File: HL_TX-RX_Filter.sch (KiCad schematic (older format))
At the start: 167 parts, among them J1 ICSP, Q1 2N7002, Q2 2N7002, Q3 2N7002, Q4 2N7002, Q5 2N7002, Q6 2N7002, Q7 2N7002, Q8 2N7002, U1 LD1117S33TR, U10 PE4259, U11 PE4259, U12 PE4259, U13 PE4259, U14 PE4259, U2 ATMEGA328-AU, U3 PE4259, U4 PE4259, U5 PE4259, U6 PE4259, U7 PE4259, U8 PE4259, U9 PE4259

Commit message: Changes to ISP wiring
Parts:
- removed D18: D_Schottky, symbol D_Schottky
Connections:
- net labels added: +3v3
- net labels removed: +5V
- wire segments 314 -> 315
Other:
- moved on the sheet: C37, C38, C39, C40, C41, C42, C43, C44, C45, C46, C47, C48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

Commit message: Corrections and further additions
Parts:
- removed U9: PE4259, symbol PE4259
- added J1: To Antenna, symbol CONN_01X02
- added J2: From Tx, symbol CONN_01X02
- added J4: To Rx in, symbol CONN_01X02
- C1: value C -> 30pF
- C10: value C -> 1000p
- C11: value C -> 15p
- C12: value C -> 39p
- C13: value C -> 68p
- C14: value C -> 82p
- C15, C28: value C -> 180p
- C16: value C -> 200p
- C17: value C -> 300p
- C18: value C -> 560p
- C19: value C -> 1082p
- C2: value C -> 78pF
- C20: value C -> 2100p
- C21: value C -> 43p
- C22: value C -> 130p
- C23: value C -> 220p
- C24: value C -> 270p
- C25: value C -> 552p
- C26: value C -> 74p
- C27: value C -> 120p
- C29: value C -> 390p
- C3: value C -> 56pF
- C30: value C -> 736p
- C39: renamed from C36; value C -> 0.1u
- C4: value C -> 150pF
- C40: renamed from C37; value C -> 3000p
- C41: renamed from C38; value C -> 0.012u
- C42: renamed from C39; value C -> 1600p
- C43: renamed from C40; value C -> 1500p
- C47: renamed from C44; value C -> 2400p
- C48: renamed from C45; value C -> 8200p
- C5: value C -> 10pF
- C52: renamed from C49; value C -> 1800p
- C53: renamed from C50; value C -> 680p
- C57: renamed from C54; value C -> 3000p
- C58: renamed from C55; value C -> 2700p
- C6: value C -> 100p
- C62: renamed from C59; value C -> 2400p
- C63: renamed from C60; value C -> 2000p
- C7: value C -> 150p
- C8: value C -> 280p
- C9: value C -> 540p
- L1: value L -> T37-10 10t
- L10: value L -> Choke
- L15: value L -> 11t
- L16, L4: value L -> 12t
- L17, L5: value L -> 15t
- L19, L26: value L -> 34t
- L2: value L -> T37-10 11t
- L25: value L -> 28t
- L27: value L -> 20t
- L31: value L -> 35t
- L32: value L -> 23t
- L6: value L -> 18t
- L8: value L -> 39t
- renumbered C64 to C34, C65 to C35, C34 to C36, C66 to C37, C35 to C38, C41 to C44, C42 to C45, C43 to C46, C46 to C49, C47 to C50, C48 to C51, C51 to C54, C52 to C55, C53 to C56, C56 to C59, C57 to C60, C58 to C61, C61 to C64, C62 to C65, C63 to C66, D23 to D10, D17 to D11, D19 to D12, D7 to D13, D8 to D14, D9 to D15, D10 to D16, D11 to D17, D12 to D18, D13 to D19, D14 to D20, D15 to D21, D16 to D22, D20 to D7, D21 to D8, D22 to D9, J1 to J3, R4 to R10, R5 to R11, R6 to R12, R7 to R13, R8 to R14, R9 to R15, R10 to R16, R11 to R17, R12 to R18, R13 to R19, R17 to R2, R15 to R20, R18 to R3, R19 to R4, R20 to R5, R14 to R6, R16 to R7, R2 to R8, R3 to R9, U11 to U10, U12 to U11, U13 to U12, U14 to U13, U10 to U9
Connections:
- net GND: now also J1.2 (P2), J2.2 (P2), J4.2 (P2)
- net at U3.3: now also U4.1
- net at C39.2, U3.5: no longer U4.5
- net at C1.2, C3.1, L1.2: now also J1.1 (P1)
- net at C33.2: now also J2.1 (P1)
- net Rx_In: no longer names the net of U5.5, U6.5, U7.5, U8.5
- net Rx_In: now also U4.5, J4.1 (P1)
- no-connect marks 24 -> 21
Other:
- moved on the sheet: C40, C41, C42, C47, C52, C57, C62, L25, L26, L31, U3, U4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

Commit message: Further progress on PCB
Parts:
- added D22: LED, symbol LED
- added D24, D25, D26, D27, D28, D29: LED, LEDs:LED_1206, symbol LED
- added R18, R22, R23, R24, R25, R26, R27: R, Resistors_SMD:R_1206_HandSoldering, symbol R
- C1, C10, C11, C12, C13, C14, C15, C16, C17, C18, C19, C2, C20, C21, C22, C23, C24, C25, C26, C27, C28, C29, C3, C30, C31, C32, C33, C34, C36, C38, C39, C4, C40, C41, C42, C43, C47, C48, C5, C52, C53, C57, C58, C6, C62, C63, C7, C8, C9: footprint (none) -> Capacitors_SMD:C_1206_HandSoldering
- C35, C37: footprint (none) -> Capacitors_ThroughHole:C_Radial_D14_L25_P5
- C44, C65: value C -> 680p; footprint (none) -> Capacitors_SMD:C_1206_HandSoldering
- C45: value C -> 470p; footprint (none) -> Capacitors_SMD:C_1206_HandSoldering
- C46: value C -> 270p; footprint (none) -> Capacitors_SMD:C_1206_HandSoldering
- C49: value C -> 3900p; footprint (none) -> Capacitors_SMD:C_1206_HandSoldering
- C50: value C -> 2400p; footprint (none) -> Capacitors_SMD:C_1206_HandSoldering
- C51: value C -> 1500p; footprint (none) -> Capacitors_SMD:C_1206_HandSoldering
- C54: value C -> 340p; footprint (none) -> Capacitors_SMD:C_1206_HandSoldering
- C55: value C -> 236p; footprint (none) -> Capacitors_SMD:C_1206_HandSoldering
- C56: value C -> 130p; footprint (none) -> Capacitors_SMD:C_1206_HandSoldering
- C59: value C -> 1220p; footprint (none) -> Capacitors_SMD:C_1206_HandSoldering
- C60: value C -> 780p; footprint (none) -> Capacitors_SMD:C_1206_HandSoldering
- C61: value C -> 510p; footprint (none) -> Capacitors_SMD:C_1206_HandSoldering
- C64: value C -> 1000p; footprint (none) -> Capacitors_SMD:C_1206_HandSoldering
- C66: value C -> 360p; footprint (none) -> Capacitors_SMD:C_1206_HandSoldering
- D10, D11, D12, D7, D8, D9: footprint (none) -> LEDs:LED_1206
- L28: value L -> 14t
- L29: value L -> 13t
- L30: value L -> 10t
- L33: value L -> 16t
- L34: value L -> 15t
- L35: value L -> 11t
- R1, R10, R11, R12, R13, R14, R15, R16, R17, R2, R3, R4, R5, R6, R7, R8, R9: footprint (none) -> Resistors_SMD:R_1206_HandSoldering
- R19: renamed from R18; footprint (none) -> Resistors_SMD:R_1206_HandSoldering
- R20: renamed from R19; footprint (none) -> Resistors_SMD:R_1206_HandSoldering
- R21: renamed from R20; footprint (none) -> Resistors_SMD:R_1206_HandSoldering
- U2: footprint TQFP32 -> Housings_QFP:TQFP-32_7x7mm_Pitch0.8mm
- renumbered D22 to D23
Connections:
- net GND: now also D22.1 (K), D24.1 (K), D25.1 (K), D26.1 (K), D27.1 (K), D28.1 (K), D29.1 (K)
- net R0: now also R27.1
- net R1: now also R22.1
- net R2: now also R23.1
- net R3: now also R24.1
- net R4: now also R25.1
- net R5: now also R26.1
- net Tptt: now also R18.1
- new net: D25.2 (A), R23.2
- new net: D24.2 (A), R22.2
- new net: D26.2 (A), R24.2
- new net: D27.2 (A), R25.2
- new net: D28.2 (A), R26.2
- new net: D29.2 (A), R27.2
- new net: D22.2 (A), R18.2

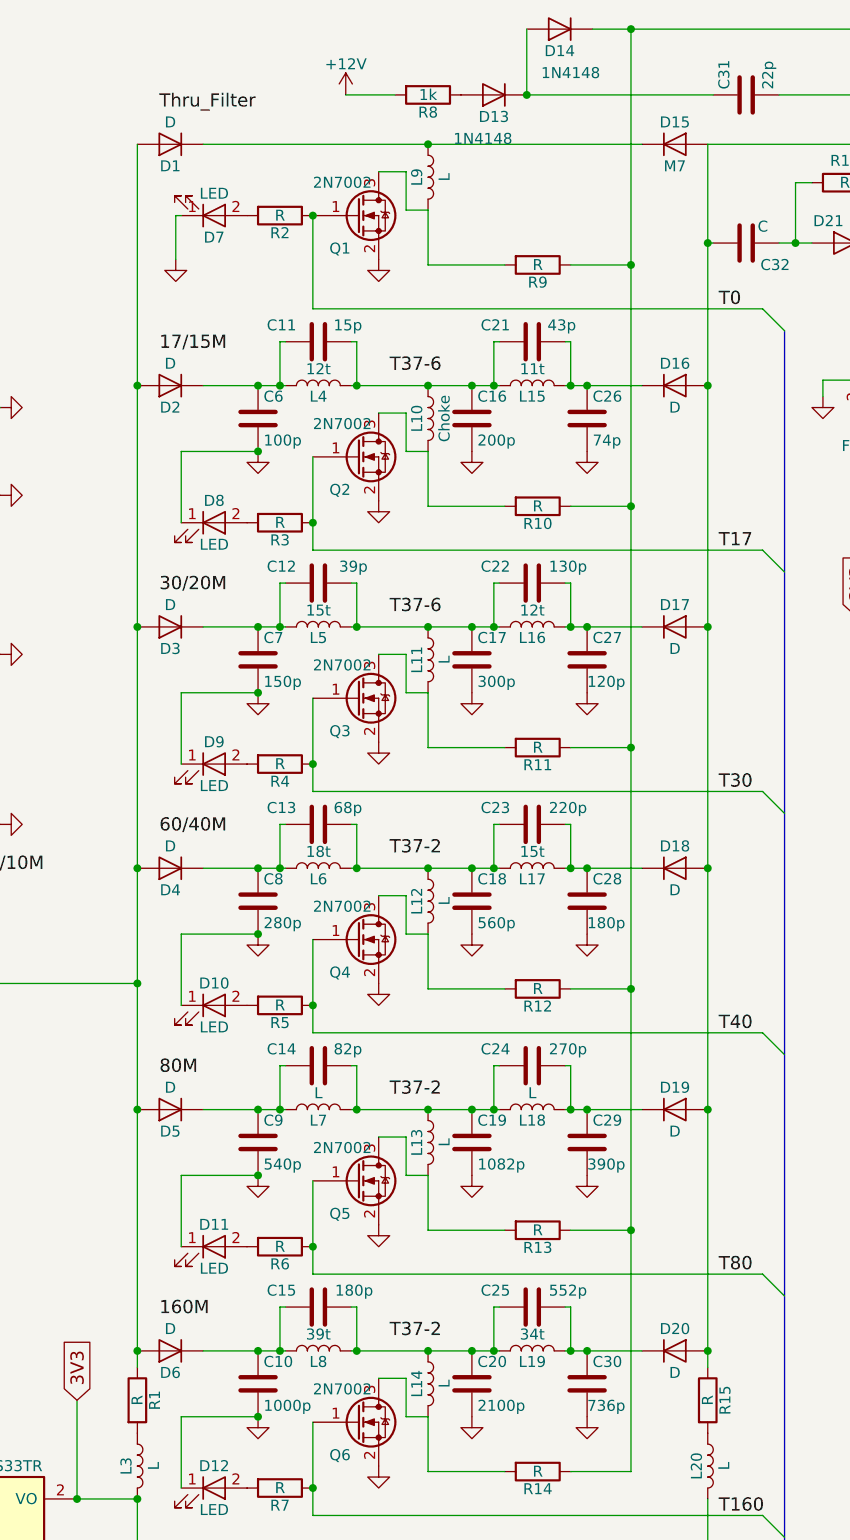
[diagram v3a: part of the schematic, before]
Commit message: Linked footprints with CvPcb
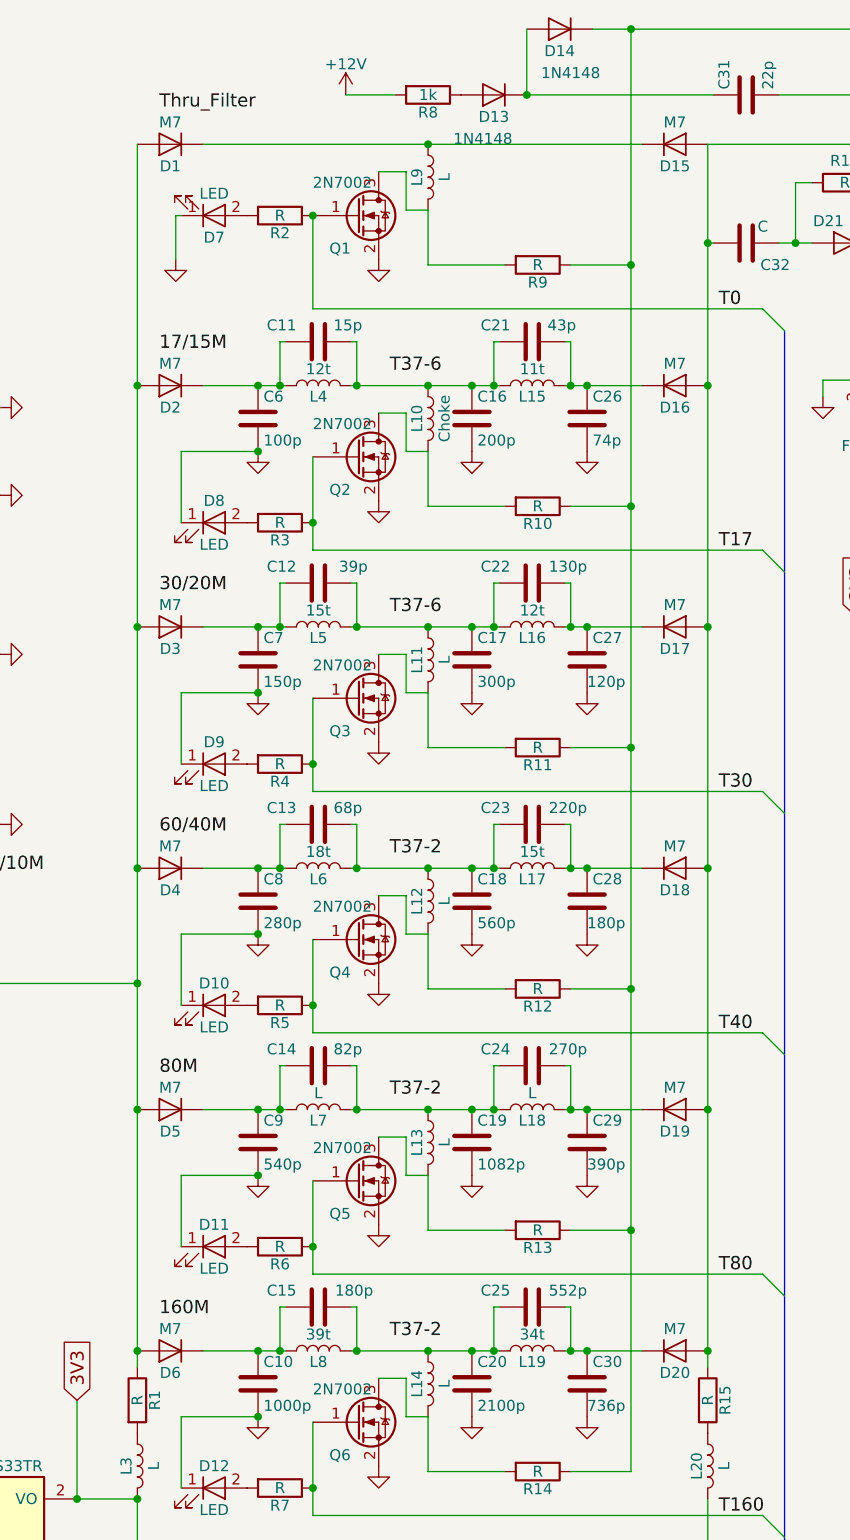
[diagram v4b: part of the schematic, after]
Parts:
- D1, D16, D17, D18, D19, D2, D20, D3, D4, D5, D6: value D -> M7; footprint (none) -> Diodes_SMD:SMB_Handsoldering
- D13, D14: footprint (none) -> Diodes_SMD:MELF_Handsoldering
- D15, D21, D23: footprint (none) -> Diodes_SMD:SMB_Handsoldering
- D22: footprint (none) -> LEDs:LED_1206
- J1, J2, J4: footprint (none) -> Pin_Headers:Pin_Header_Straight_1x02
- J3: footprint (none) -> Pin_Headers:Pin_Header_Straight_1x06
- L1, L15, L16, L17, L19, L2, L25, L26, L27, L28, L29, L30, L31, L32, L33, L34, L35, L4, L5, L6, L8: footprint (none) -> Inductors:Toroid_T37_Vertical
- L10, L11, L12, L13, L14, L18, L20, L21, L22, L23, L24, L3, L7, L9: footprint (none) -> Pin_Headers:Pin_Header_Straight_1x02_Pitch3.96mm_Friction_Lock
- Q1, Q2, Q3, Q4, Q5, Q6, Q7, Q8: footprint (none) -> TO_SOT_Packages_SMD:SOT-23
- U10, U11, U12, U13, U3, U4, U5, U6, U7, U8, U9: footprint (none) -> TO_SOT_Packages_SMD:SC-70-6

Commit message: Progressing with board layout
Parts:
- added J4: Data In, Pin_Headers:Pin_Header_Straight_1x04, symbol CONN_01X04
- added J5: SCL SDA, Pin_Headers:Pin_Header_Straight_1x02, symbol CONN_01X02
- C35, C37: footprint Capacitors_ThroughHole:C_Radial_D14_L25_P5 -> Capacitors_ThroughHole:C_Radial_D5_L11_P2
- L18: value L -> 19t; footprint Pin_Headers:Pin_Header_Straight_1x02_Pitch3.96mm_Friction_Lock -> Inductors:Toroid_T37_Vertical
- L7: value L -> 22t; footprint Pin_Headers:Pin_Header_Straight_1x02_Pitch3.96mm_Friction_Lock -> Inductors:Toroid_T37_Vertical
- R21: value R -> 10k
- renumbered J4 to J6
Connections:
- net at C40.2, C42.1: now also L25.2; no longer L25.1
- net at C41.1: now also L25.1; no longer L25.2
- net at C46.2, C56.1: now also L30.2; no longer L30.1
- net at C51.1: now also L30.1; no longer L30.2
- net at C15.2, C20.1, C25.1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: now also L8.1; no longer L8.2
- net at C10.1, C15.1, D6.1 (K): now also L8.2; no longer L8.1
- net at C14.2, C19.1, C24.1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: now also L7.1; no longer L7.2
- net at C14.1, C9.1, D5.1 (K): now also L7.2; no longer L7.1
- net at C13.2, C18.1, C23.1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: now also L6.1; no longer L6.2
- net at C13.1, C8.1, D4.1 (K): now also L6.2; no longer L6.1
- net at C12.2, C17.1, C22.1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: now also L5.1; no longer L5.2
- net at C12.1, C7.1, D3.1 (K): now also L5.2; no longer L5.1
- net at C11.2, C16.1, C21.1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: now also L4.1; no longer L4.2
- net at C11.1, C6.1, D2.1 (K): now also L4.2; no longer L4.1
- net at U2.23 ((PCINT8/ADC0)PC0): now also J4.1 (P1)
- net at U2.24 ((PCINT9/ADC1)PC1): now also J4.2 (P2)
- net at U2.25 ((PCINT10/ADC2)PC2): now also J4.3 (P3)
- net at U2.26 ((PCINT11/ADC3)PC3): now also J4.4 (P4)
- net at U2.27 ((PCINT12/SDA/ADC4)PC4): now also J5.1 (P1)
- net at U2.28 ((PCINT13/SCL/ADC5)PC5): now also J5.2 (P2)
- net at C45.2, C55.1: now also L29.2; no longer L29.1
- net at C50.1: now also L29.1; no longer L29.2
- net at C44.2, C54.1: now also L28.2; no longer L28.1
- net at C49.1: now also L28.1; no longer L28.2
- net at C43.2, C53.1: now also L27.2; no longer L27.1
- net at C48.1: now also L27.1; no longer L27.2
- no-connect marks 21 -> 15
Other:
- moved on the sheet: L25, L27, L28, L29, L30, L4, L5, L6, L7, L8, R21
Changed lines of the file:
@@
 F 3 "" H 8975 950 50  0001 C CNN
 	1    8975 950
-	1    0    0    -1
+	-1   0    0    1
 $EndComp
 $Comp
@@
 F 3 "" H 9425 6050 50  0001 C CNN
 	1    9425 6050
-	1    0    0    -1
+	-1   0    0    1
 $EndComp
 $Comp
@@
 F 3 "" H 2775 6625 50  0001 C CNN
 	1    2775 6625
-	0    -1   -1   0
+	0    1    1    0
 $EndComp
 $Comp
@@
 P 3750 5525
 F 0 "L18" V 3700 5525 50  0000 C CNN
-F 1 "L" V 3825 5525 50  0000 C CNN
-F 2 "Pin_Headers:Pin_Header_Straight_1x02_Pitch3.96mm_Friction_Lock" H 3750 5525 50  0001 C CNN
+F 1 "19t" V 3825 5525 50  0000 C CNN
+F 2 "Inductors:Toroid_T37_Vertical" H 3750 5525 50  0001 C CNN
 F 3 "" H 3750 5525 50  0001 C CNN
 	1    3750 5525
@@
 P 2775 5525
 F 0 "L7" V 2725 5525 50  0000 C CNN
-F 1 "L" V 2850 5525 50  0000 C CNN
-F 2 "Pin_Headers:Pin_Header_Straight_1x02_Pitch3.96mm_Friction_Lock" H 2775 5525 50  0001 C CNN
+F 1 "22t" V 2850 5525 50  0000 C CNN
+F 2 "Inductors:Toroid_T37_Vertical" H 2775 5525 50  0001 C CNN
 F 3 "" H 2775 5525 50  0001 C CNN
 	1    2775 5525
-	0    -1   -1   0
+	0    1    1    0
 $EndComp
 $Comp
@@
 F 3 "" H 2775 4425 50  0001 C CNN
 	1    2775 4425
-	0    -1   -1   0
+	0    1    1    0
 $EndComp
 $Comp
@@
 F 3 "" H 2775 3325 50  0001 C CNN
 	1    2775 3325
-	0    -1   -1   0
+	0    1    1    0
 $EndComp
 $Comp
@@
 F 3 "" H 2775 2225 50  0001 C CNN
 	1    2775 2225
-	0    -1   -1   0
+	0    1    1    0
 $EndComp
 $Comp
@@
 F 3 "" H 9425 5000 50  0001 C CNN
 	1    9425 5000
-	1    0    0    -1
+	-1   0    0    1
 $EndComp
 $Comp
@@
 F 3 "" H 9425 3950 50  0001 C CNN
 	1    9425 3950
-	1    0    0    -1
+	-1   0    0    1
 $EndComp
 $Comp
@@
 F 3 "" H 9425 2900 50  0001 C CNN
 	1    9425 2900
-	1    0    0    -1
+	-1   0    0    1
 $EndComp
 $Comp
@@
 L R R21
 U 1 1 591F094F
-P 7725 5200
-F 0 "R21" V 7805 5200 50  0000 C CNN
-F 1 "R" V 7725 5200 50  0000 C CNN
-F 2 "Resistors_SMD:R_1206_HandSoldering" V 7655 5200 50  0001 C CNN
-F 3 "" H 7725 5200 50  0001 C CNN
-	1    7725 5200
+P 7750 5300
+F 0 "R21" V 7830 5300 50  0000 C CNN
+F 1 "10k" V 7750 5300 50  0000 C CNN
+F 2 "Resistors_SMD:R_1206_HandSoldering" V 7680 5300 50  0001 C CNN
+F 3 "" H 7750 5300 50  0001 C CNN
+	1    7750 5300
 	0    1    1    0
 $EndComp
@@
 F 0 "C35" H 6025 3300 50  0000 L CNN
 F 1 "4.7u" H 6025 3100 50  0000 L CNN
-F 2 "Capacitors_ThroughHole:C_Radial_D14_L25_P5" H 6000 3200 50  0001 C CNN
+F 2 "Capacitors_ThroughHole:C_Radial_D5_L11_P2" H 6000 3200 50  0001 C CNN
 F 3 "" H 6000 3200 50  0001 C CNN
 	1    6000 3200
@@
 F 0 "C37" H 6325 3300 50  0000 L CNN
 F 1 "4.7u" H 6325 3100 50  0000 L CNN
-F 2 "Capacitors_ThroughHole:C_Radial_D14_L25_P5" H 6300 3200 50  0001 C CNN
+F 2 "Capacitors_ThroughHole:C_Radial_D5_L11_P2" H 6300 3200 50  0001 C CNN
 F 3 "" H 6300 3200 50  0001 C CNN
 	1    6300 3200
@@
 NoConn ~ 5400 5200
 NoConn ~ 5400 4350
-NoConn ~ 7300 4600
-NoConn ~ 7300 4700
-NoConn ~ 7300 4800
-NoConn ~ 7300 4900
-NoConn ~ 7300 5000
-NoConn ~ 7300 5100
 NoConn ~ 7300 5350
 NoConn ~ 7300 5450
@@
 Text Label 7650 3450 0    60   ~ 0
 MOSI
-Text GLabel 7875 5000 1    60   Input ~ 0
+Text GLabel 7900 5400 3    60   Input ~ 0
 3V3
 Text Label 3100 2175 0    60   ~ 0
@@
 $EndComp
 $Comp
-L CONN_01X02 J4
+L CONN_01X02 J6
 U 1 1 596713D0
 P 8150 3100
-F 0 "J4" V 8150 3250 50  0000 C CNN
+F 0 "J6" V 8150 3250 50  0000 C CNN
 F 1 "To Rx in" V 8250 3100 50  0000 C CNN
 F 2 "Pin_Headers:Pin_Header_Straight_1x02" H 8150 3100 50  0001 C CNN
@@
 Connection ~ 6000 3050
 Wire Wire Line
-	7300 5200 7575 5200
+	7300 5200 7600 5200
 Wire Wire Line
 	2150 7250 2150 6925
@@
 	5700 2675 7500 2675
 Wire Wire Line
-	7875 5000 7875 5200
+	7900 5400 7900 5300
 Wire Wire Line
 	1125 2325 1325 2325
@@
 	5825 2475 5600 2475
 Connection ~ 5600 2475
+$Comp
+L CONN_01X02 J5
+U 1 1 5967F9A2
+P 7900 5050
+F 0 "J5" H 7900 5200 50  0000 C CNN
+F 1 "SCL SDA" V 8000 5050 50  0000 C CNN
+F 2 "Pin_Headers:Pin_Header_Straight_1x02" H 7900 5050 50  0001 C CNN
+F 3 "" H 7900 5050 50  0001 C CNN
+	1    7900 5050
+	1    0    0    -1
+$EndComp
+Wire Wire Line
+	7300 5000 7700 5000
+Wire Wire Line
+	7300 5100 7700 5100
+$Comp
+L CONN_01X04 J4
+U 1 1 596806D9
+P 7575 4750
+F 0 "J4" H 7575 5000 50  0000 C CNN
+F 1 "Data In" V 7675 4750 50  0000 C CNN
+F 2 "Pin_Headers:Pin_Header_Straight_1x04" H 7575 4750 50  0001 C CNN
+F 3 "" H 7575 4750 50  0001 C CNN
+	1    7575 4750
+	1    0    0    -1
+$EndComp
+Wire Wire Line
+	7300 4600 7375 4600
+Wire Wire Line
+	7300 4700 7375 4700
+Wire Wire Line
+	7300 4800 7375 4800
+Wire Wire Line
+	7300 4900 7375 4900
+Wire Wire Line
+	7600 5200 7600 5300
+Connection ~ 8525 6150
+Connection ~ 8525 5950
+Connection ~ 8525 5100
+Connection ~ 8525 4900
+Connection ~ 8525 4050
+Connection ~ 8525 3850
+Connection ~ 8525 2800
 $EndSCHEMATC

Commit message: Resized toroids and M7 diodes
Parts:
- C35, C37: footprint Capacitors_ThroughHole:C_Radial_D5_L11_P2 -> Capacitors_THT:CP_Radial_D5.0mm_P2.00mm
- D1, D15, D16, D17, D18, D19, D2, D20, D21, D23, D3, D4, D5, D6: footprint Diodes_SMD:SMB_Handsoldering -> Diodes_SMD:D_SMA_Handsoldering
- L1, L15, L16, L17, L18, L19, L2, L25, L26, L27, L28, L29, L30, L31, L32, L33, L34, L35, L4, L5, L6, L7, L8: footprint Inductors:Toroid_T37_Vertical -> Inductors_G:Toroid_T37_Vertical

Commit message: More Tx layout and choke footprint mods
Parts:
- L10, L11, L12, L13, L14, L20, L21, L22, L23, L24, L3, L9: footprint Pin_Headers:Pin_Header_Straight_1x02_Pitch3.96mm_Friction_Lock -> Inductors_G:BalunCoreChoke
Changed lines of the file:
@@
 F 0 "L14" V 3225 6775 50  0000 C CNN
 F 1 "L" V 3350 6775 50  0000 C CNN
-F 2 "Pin_Headers:Pin_Header_Straight_1x02_Pitch3.96mm_Friction_Lock" H 3275 6775 50  0001 C CNN
+F 2 "Inductors_G:BalunCoreChoke" H 3275 6775 50  0001 C CNN
 F 3 "" H 3275 6775 50  0001 C CNN
 	1    3275 6775
@@
 F 0 "L3" V 1900 7150 50  0000 C CNN
 F 1 "L" V 2025 7150 50  0000 C CNN
-F 2 "Pin_Headers:Pin_Header_Straight_1x02_Pitch3.96mm_Friction_Lock" H 1950 7150 50  0001 C CNN
+F 2 "Inductors_G:BalunCoreChoke" H 1950 7150 50  0001 C CNN
 F 3 "" H 1950 7150 50  0001 C CNN
 	1    1950 7150
@@
 F 0 "L20" V 4500 7150 50  0000 C CNN
 F 1 "L" V 4625 7150 50  0000 C CNN
-F 2 "Pin_Headers:Pin_Header_Straight_1x02_Pitch3.96mm_Friction_Lock" H 4550 7150 50  0001 C CNN
+F 2 "Inductors_G:BalunCoreChoke" H 4550 7150 50  0001 C CNN
 F 3 "" H 4550 7150 50  0001 C CNN
 	1    4550 7150
@@
 F 0 "L13" V 3225 5675 50  0000 C CNN
 F 1 "L" V 3350 5675 50  0000 C CNN
-F 2 "Pin_Headers:Pin_Header_Straight_1x02_Pitch3.96mm_Friction_Lock" H 3275 5675 50  0001 C CNN
+F 2 "Inductors_G:BalunCoreChoke" H 3275 5675 50  0001 C CNN
 F 3 "" H 3275 5675 50  0001 C CNN
 	1    3275 5675
@@
 F 0 "L12" V 3225 4575 50  0000 C CNN
 F 1 "L" V 3350 4575 50  0000 C CNN
-F 2 "Pin_Headers:Pin_Header_Straight_1x02_Pitch3.96mm_Friction_Lock" H 3275 4575 50  0001 C CNN
+F 2 "Inductors_G:BalunCoreChoke" H 3275 4575 50  0001 C CNN
 F 3 "" H 3275 4575 50  0001 C CNN
 	1    3275 4575
@@
 F 0 "L11" V 3225 3475 50  0000 C CNN
 F 1 "L" V 3350 3475 50  0000 C CNN
-F 2 "Pin_Headers:Pin_Header_Straight_1x02_Pitch3.96mm_Friction_Lock" H 3275 3475 50  0001 C CNN
+F 2 "Inductors_G:BalunCoreChoke" H 3275 3475 50  0001 C CNN
 F 3 "" H 3275 3475 50  0001 C CNN
 	1    3275 3475
@@
 F 0 "L10" V 3225 2375 50  0000 C CNN
 F 1 "Choke" V 3350 2375 50  0000 C CNN
-F 2 "Pin_Headers:Pin_Header_Straight_1x02_Pitch3.96mm_Friction_Lock" H 3275 2375 50  0001 C CNN
+F 2 "Inductors_G:BalunCoreChoke" H 3275 2375 50  0001 C CNN
 F 3 "" H 3275 2375 50  0001 C CNN
 	1    3275 2375
@@
 F 0 "L9" V 3225 1275 50  0000 C CNN
 F 1 "L" V 3350 1275 50  0000 C CNN
-F 2 "Pin_Headers:Pin_Header_Straight_1x02_Pitch3.96mm_Friction_Lock" H 3275 1275 50  0001 C CNN
+F 2 "Inductors_G:BalunCoreChoke" H 3275 1275 50  0001 C CNN
 F 3 "" H 3275 1275 50  0001 C CNN
 	1    3275 1275
@@
 F 0 "L24" V 7075 1675 50  0000 C CNN
 F 1 "Choke" V 6925 1600 50  0000 C CNN
-F 2 "Pin_Headers:Pin_Header_Straight_1x02_Pitch3.96mm_Friction_Lock" H 7000 1575 50  0001 C CNN
+F 2 "Inductors_G:BalunCoreChoke" H 7000 1575 50  0001 C CNN
 F 3 "" H 7000 1575 50  0001 C CNN
 	1    7000 1575
@@
 F 0 "L22" V 5750 1650 50  0000 C CNN
 F 1 "Choke" V 5600 1600 50  0000 C CNN
-F 2 "Pin_Headers:Pin_Header_Straight_1x02_Pitch3.96mm_Friction_Lock" H 5675 1575 50  0001 C CNN
+F 2 "Inductors_G:BalunCoreChoke" H 5675 1575 50  0001 C CNN
 F 3 "" H 5675 1575 50  0001 C CNN
 	1    5675 1575
@@
 F 0 "L23" V 6300 2100 50  0000 C CNN
 F 1 "Choke" V 6425 2100 50  0000 C CNN
-F 2 "Pin_Headers:Pin_Header_Straight_1x02_Pitch3.96mm_Friction_Lock" H 6350 2100 50  0001 C CNN
+F 2 "Inductors_G:BalunCoreChoke" H 6350 2100 50  0001 C CNN
 F 3 "" H 6350 2100 50  0001 C CNN
 	1    6350 2100
@@
 F 0 "L21" V 5625 1300 50  0000 C CNN
 F 1 "Choke" V 5750 1300 50  0000 C CNN
-F 2 "Pin_Headers:Pin_Header_Straight_1x02_Pitch3.96mm_Friction_Lock" H 5675 1300 50  0001 C CNN
+F 2 "Inductors_G:BalunCoreChoke" H 5675 1300 50  0001 C CNN
 F 3 "" H 5675 1300 50  0001 C CNN
 	1    5675 1300
